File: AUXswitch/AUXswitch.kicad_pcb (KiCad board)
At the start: 2 copper layers, 25 parts, among them J1 Conn_02x04_Counter_Clockwise, J10 5V_IN, J2 Conn_01x03, J3 INPUT_1, J4 INPUT_2, J5 OUTPUT, J6 LIVE_IN, J7 LIVE_OUT, J9 LIVE_OUT_SMP, K1 HRS2H-S-DC5V-N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

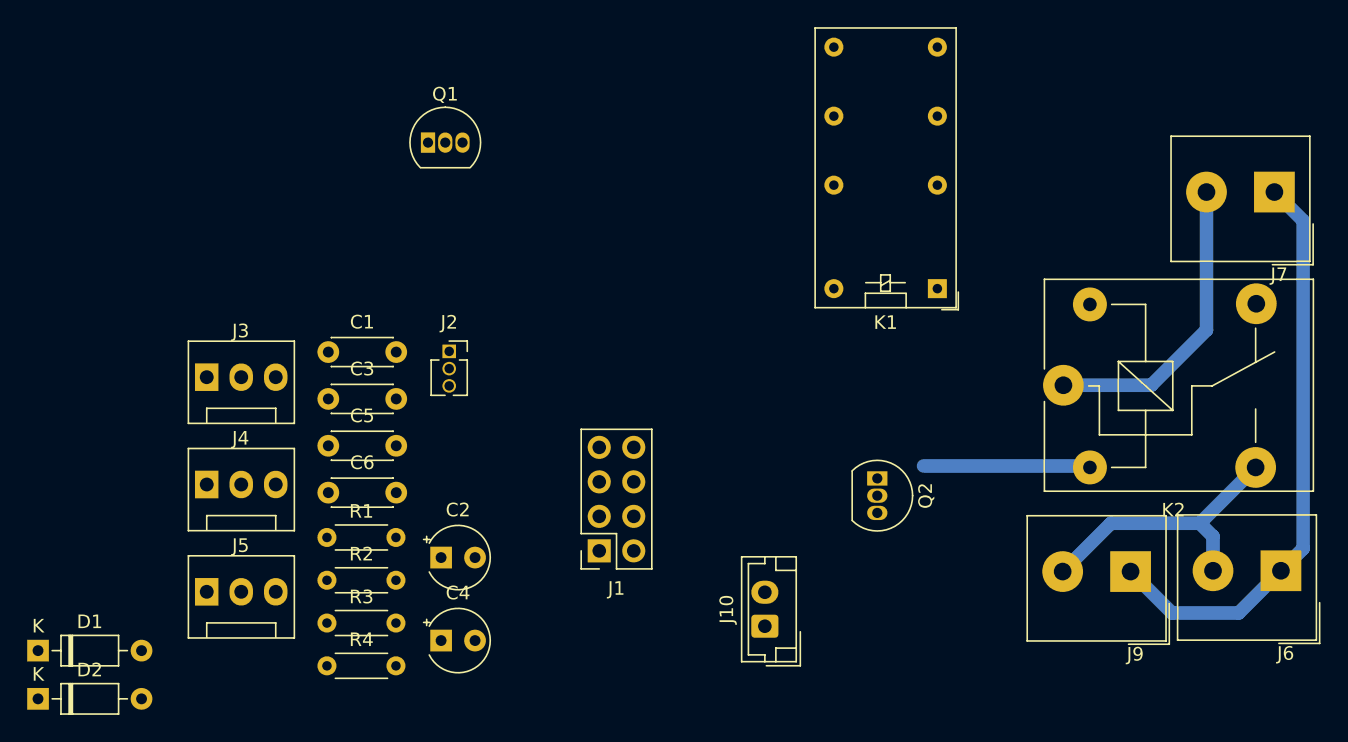
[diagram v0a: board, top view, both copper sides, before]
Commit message: fixede pinouts
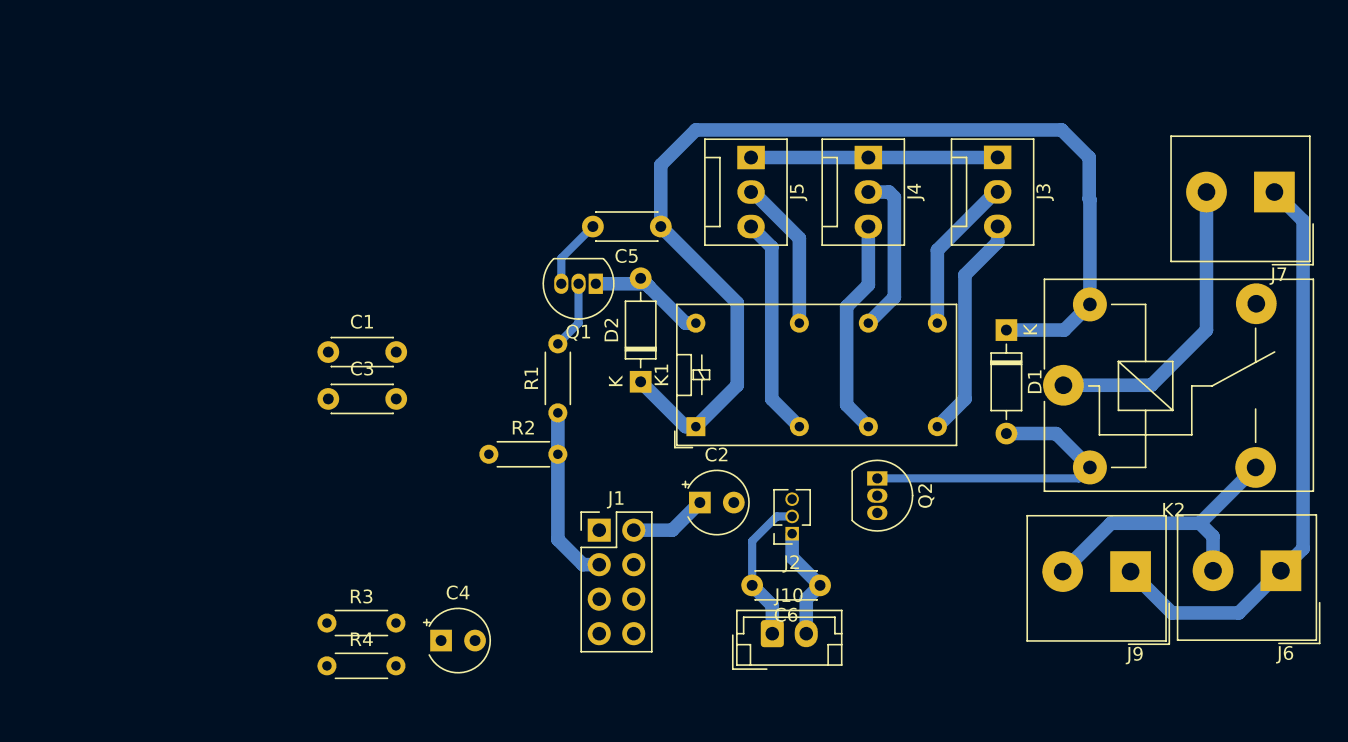
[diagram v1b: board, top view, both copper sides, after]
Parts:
- J1: value Conn_02x04_Counter_Clockwise -> Conn_02x04_Odd_Even; footprint Connector_PinSocket_2.54mm:PinSocket_2x04_P2.54mm_Vertical -> Connector_PinHeader_2.54mm:PinHeader_2x04_P2.54mm_Vertical
- moved D1 75.1 mm to (120.9, 67.6), turned to -90 degrees
- moved J3 60.4 mm to (120.3, 54.9), turned to -90 degrees
- moved J4 54.3 mm to (110.7, 54.9), turned to -90 degrees
- moved J5 51.3 mm to (102.1, 54.9), turned to -90 degrees
- moved D2 50.1 mm to (94.0, 71.4), turned to 90 degrees
- moved C6 36.8 mm to (107.2, 86.4), turned to 180 degrees
- moved C5 29.3 mm to (95.5, 59.9), turned to 180 degrees
- moved J2 28.6 mm to (105.1, 82.6), turned to 180 degrees
- moved K1 20.5 mm to (98.0, 74.7), turned to 90 degrees
- moved C2 19.5 mm to (98.3, 80.3)
- moved R1 19.3 mm to (87.9, 73.7), turned to 90 degrees
- moved Q1 16.1 mm to (90.7, 64.2), turned to 180 degrees
- moved R2 15.1 mm to (82.8, 76.7)
- moved J1 1.52 mm to (90.9, 82.3), turned to 0 degrees
- moved J10 0.77 mm to (103.7, 89.9), turned to 0 degrees
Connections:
- J1 pad 2: GPIO_0 -> +3.3V
- J1 pad 3: GPIO_2 -> AUX_pin
- J1 pad 4: GND -> Reset
- J1 pad 5: TxD -> AMP_pin
- J1 pad 7: Reset -> GND
- J1 pad 8: +3.3V -> TxD
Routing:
- net +5V: track 0.00 -> 88.0 mm
- net GNDA: track 0.00 -> 18.2 mm
- net IN1_R: track 0.00 -> 16.6 mm
- net GND: track 0.00 -> 16.3 mm
- net OUT_R: track 0.00 -> 16.2 mm
- net IN2_R: track 0.00 -> 16.1 mm
- net AUX_pin: track 0.00 -> 13.1 mm
- net IN2_L: track 0.00 -> 12.1 mm
- net IN1_L: track 0.00 -> 11.6 mm
- net OUT_L: track 0.00 -> 11.2 mm
- net Net-(D1-A): track 12.3 -> 23.2 mm
- net Net-(D2-A): track 0.00 -> 9.31 mm
- net +3.3V: track 0.00 -> 5.71 mm
- net Net-(Q1-B): track 0.00 -> 5.06 mm
